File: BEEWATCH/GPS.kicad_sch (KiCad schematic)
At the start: 6 parts, among them Q1 Si1442DH, U3 L80-R

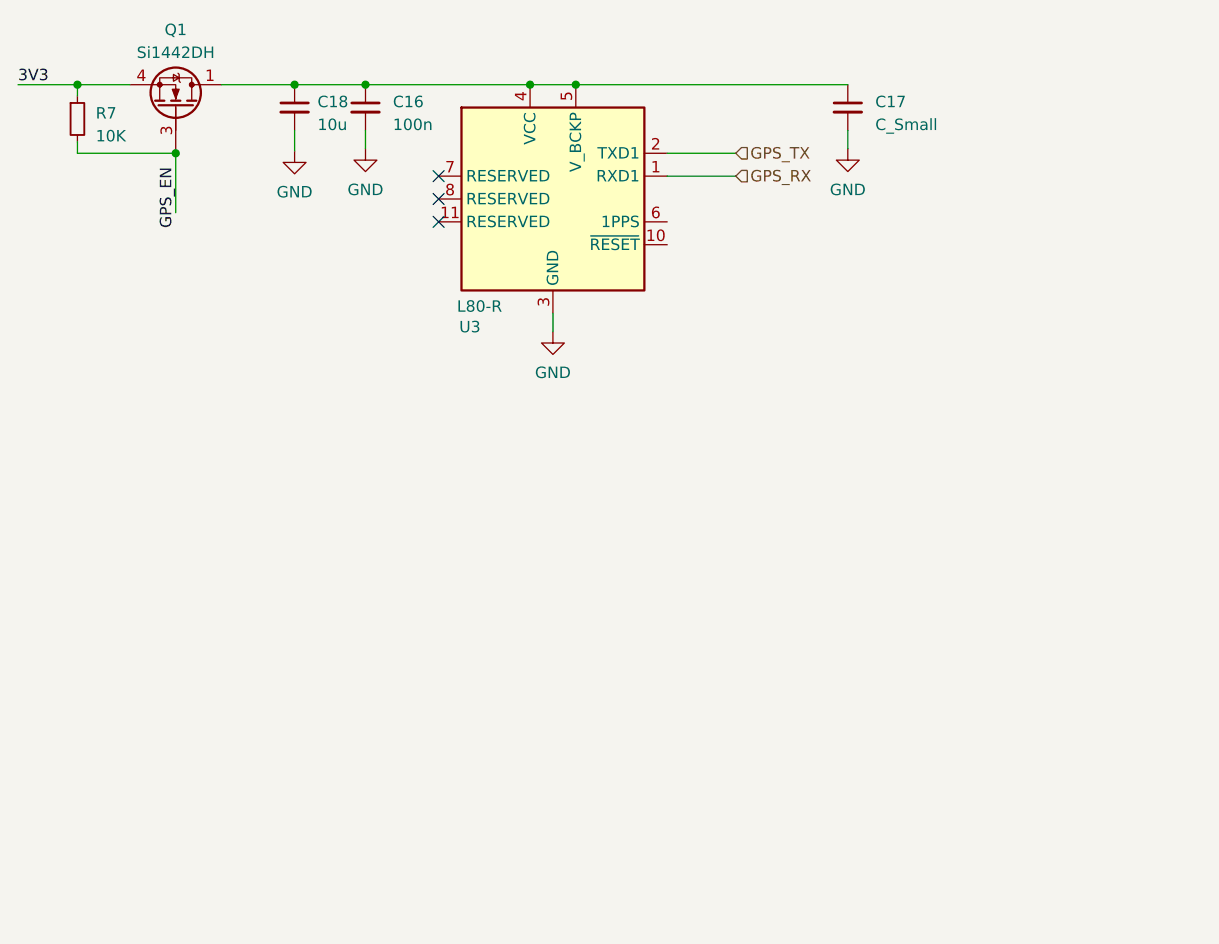
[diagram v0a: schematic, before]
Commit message: GPS Removed
GPS is expensive and difficult to find small factor foot print. So No GPS function
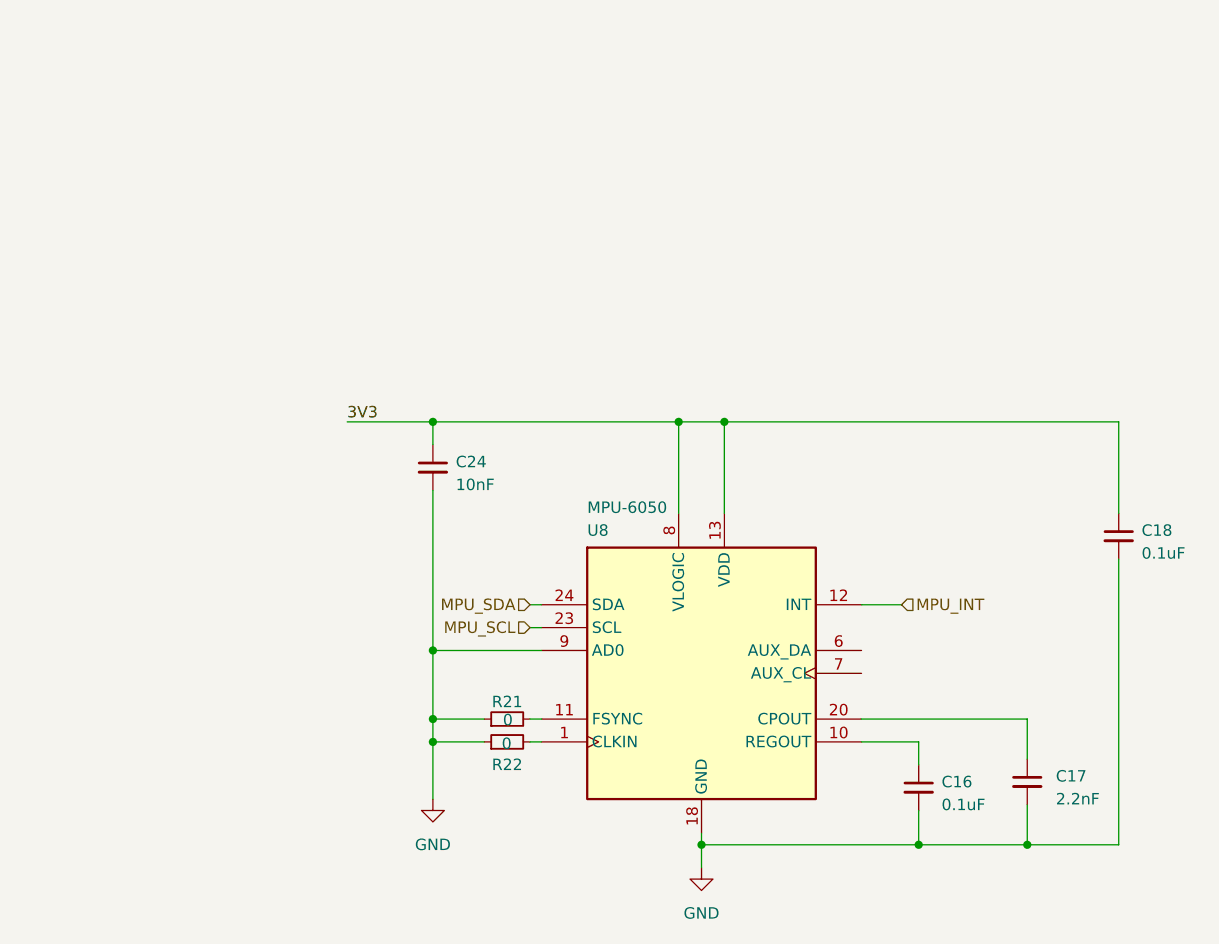
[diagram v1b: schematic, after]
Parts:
- removed Q1: Si1442DH, Package_TO_SOT_SMD:SOT-363_SC-70-6, symbol Transistor_FET:Si1442DH
- removed R7: 10K, symbol Device:R_Small
- removed U3: L80-R, RF_GPS:Quectel_L80-R, symbol RF_GPS:L80-R
- added C24: 10nF, symbol Device:C_Small
- added R21, R22: 0, symbol Device:R_Small
- added U8: MPU-6050, Sensor_Motion:InvenSense_QFN-24_4x4mm_P0.5mm, symbol Sensor_Motion:MPU-6050
- C16: value 100n -> 0.1uF
- C17: value C_Small -> 2.2nF
- C18: value 10u -> 0.1uF
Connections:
- net 3V3: now also C18.1, C24.1, U8.13 (VDD), U8.8 (VLOGIC)
- net GND: now also C24.2, R21.1, R22.1, U8.18 (GND), U8.9 (AD0)
- new net: C17.1, U8.20 (CPOUT)
- new net: C16.1, U8.10 (REGOUT)
- new net: R22.2, U8.1 (CLKIN)
- new net: R21.2, U8.11 (FSYNC)
- new net MPU_INT: U8.12 (INT)
- new net MPU_SCL: U8.23 (SCL)
- new net MPU_SDA: U8.24 (SDA)
- no-connect marks 3 -> 0
